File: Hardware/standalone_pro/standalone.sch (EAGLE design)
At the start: 107 parts, among them IC1 STM32F050C6T6A, IC2 AP1212, IC3 AP1212, Q2 32.768khz, U1 NMOS_2N7002, U10 ZXCT1107SA-7, U2 DMS3016SSS-13, U3 DMS3016SSS-13, U4 LM2576S, U5 NMOS_2N7002, U6 NMOS_2N7002, U7 INA213AIDCKT, U9 PMOS_RSS090P03, X1 KUSBVX, X2 KUSBVX, X3 KUSBVX, X4 KUSBVX

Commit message: Standalone pro physical layout finalised
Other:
- note added: "Swap with 1433428C"
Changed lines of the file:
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@@
 <text x="848.36" y="81.28" size="1.778" layer="98">1A Current Limit</text>
 <text x="731.52" y="208.28" size="1.778" layer="98">Add Inv Out</text>
+<text x="259.08" y="396.24" size="1.778" layer="98" rot="R90">Swap with 1433428C</text>
 </plain>
 <instances>

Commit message: Pro Standalone board updated
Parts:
- removed GATE_DRIVE: IR2104S, equinox:IR2104S
- removed KEY_1, KEY_2, KEY_3: 10K, rcl:R-EU_M0805
- removed U$2, U$3, U$4, U$5, U$6: KYCON_KLDVX-0202, equinox:KYCON_KLDVX-0202
- removed U1: NMOS_2N7002, equinox:NMOS_2N7002
- added D1: SSB43L, equinox:DIODE_SSB43L
- added D5: BZX384-C3V6, equinox:BZX384-C3V6
- added DC1, DC2, DC3, DC4, DC5: KYCON_KLDVX-0202, equinox:KYCON_KLDVX-0202
- added IC4: AP1212, equinox:AP1212
- added PTC1: 7A, equinox:PTC_MF_R700
- added R38: 49.9k, resistor:R-EU_M0805
- added U11, U12, U8: NMOS_2N7002, equinox:NMOS_2N7002
- BATT: OC_FARNELL (none) -> 1012166
- BATT_BCKUP: OC_FARNELL (none) -> 1298246
- BUZZ1: device buzzer:BUZZ_14MM -> equinox:BUZZ_14MM
- C21: value 100u -> 100uF; OC_FARNELL (none) -> 1539489
- C22: OC_FARNELL (none) -> 1244342
- C4: OC_FARNELL (none) -> 1539489
- C5: value 0.1uF -> 100nF
- C6: OC_FARNELL (none) -> 9695877
- D2: OC_FARNELL (none) -> 9550216
- D3: value (none) -> SSB43L; OC_FARNELL (none) -> 1336556
- D4: value US1D - 1625280 -> US1D; OC_FARNELL (none) -> 1625280
- D6: OC_FARNELL (none) -> 1843695
- IC1: OC_FARNELL (none) -> 2115059
- IC2: OC_FARNELL (none) -> 1825302
- IC3: value AP1212 -> IR2104S; device equinox:AP1212 -> equinox:IR2104S; OC_FARNELL (none) -> 8638756
- KEYPAD: OC_FARNELL (none) -> 588763
- L_5V: OC_FARNELL (none) -> 1612709
- L_MPPT: OC_FARNELL (none) -> 1929706
- POW: RS (none) -> 758-1979
- Q1: OC_FARNELL (none) -> 2101358
- R1: value 1k -> 75k
- R21: value 1K -> 1k
- R29: value 75k -> 1k
- R31: value 49.9k -> 10M
- R32, R34, R36: value 75k -> 49.9k
- R33, R35, R37: value 49.9k -> 75k
- R4, R6: value 1.32k -> 1.33k
- SOL: TOBY (none) -> DC-001-A-2.1mm-R
- U2, U3: value DMS3016SSS-13 -> FDS6690a; OC_FARNELL (none) -> 9845275
- U4: OC_FARNELL (none) -> 1469178
- U9: OC_FARNELL (none) -> 1525544
- renumbered 5V_CIN to C21, 5V_COUT to C22, Q2 to Q1
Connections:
- removed net LCD_PWR: IC1.PA11, R1.2
- new net N$47: R35.1, R36.2, X4.2
- new net N$48: R37.1, R38.2, X4.3
- net +3V3: no longer KEY_1.2, KEY_2.2, KEY_3.2
- net +5V: now also IC4.IN; no longer IC3.IN
- net 12V_OUT: now also DC1.PAD1, DC2.PAD1, DC3.PAD1; no longer U$2.PAD1, U$3.PAD1, U$4.PAD1
- net 12V_OUT1: now also DC4.PAD1, DC5.PAD1; no longer U$5.PAD1, U$6.PAD1
- net GND: now also CONTR.E, D1.ANODE, D5.A, DC1.PAD2, DC1.PAD3, DC2.PAD2, DC2.PAD3, DC3.PAD2, DC3.PAD3, DC4.PAD2, DC4.PAD3, DC5.PAD2, DC5.PAD3, DIS1.D0, DIS1.D1, DIS1.D2, DIS1.D3, DIS1.GND, IC3.COM, IC4.GND, R32.1, R34.1, R36.1, R38.1, U11.S, U8.S; no longer BUZZ1.-, GATE_DRIVE.COM, IC3.GND, R31.1, R33.1, R35.1, R37.1, U$4.PAD2, U$5.PAD2, U$5.PAD3, U$6.PAD2, U$6.PAD3, U1.S
- net N$10: now also IC3.VB; no longer GATE_DRIVE.VB
- net N$13: now also IC3.LO; no longer GATE_DRIVE.LO
- net N$16: now also IC3.VCC; no longer GATE_DRIVE.VCC
- net N$17: now also R33.1, R34.2, X3.3; no longer R1.1, U1.G
- net N$22: now also R29.1; no longer BUZZ1.+
- net N$23: no longer KEY_1.1
- net N$24: no longer KEY_2.1
- net N$26: no longer KEY_3.1
- net N$3: now also IC3.SD/; no longer GATE_DRIVE.SD/
- net N$4: now also D1.CATHODE, PTC1.P$1; no longer BATTCON$1.S
- net N$42: now also BUZZ1.-, U8.D; no longer R29.1, R31.2, X3.2
- net N$43: now also R29.2, U8.G; no longer R32.1, R33.2, X3.3
- net N$44: now also C16.2, R31.2, U11.G; no longer R34.1, R35.2, X4.2
- net N$45: now also U11.D, U12.S; no longer R36.1, R37.2, X4.3
- net N$46: now also BATTCON$1.S, PTC1.P$2; no longer U$2.PAD2, U$2.PAD3, U$3.PAD2, U$3.PAD3, U$4.PAD3
- net N$5: now also R1.1, R32.2, X3.2; no longer CONTR.E, DIS1.D0, DIS1.D1, DIS1.D2, DIS1.D3, DIS1.GND, U1.D
- net N$6: now also IC3.VS; no longer GATE_DRIVE.VS
- net N$7: now also IC3.HO; no longer GATE_DRIVE.HO
- net N$8: now also IC3.IN; no longer GATE_DRIVE.IN
- net NRST: now also U12.D
- net SOL_I: now also D5.C
- net USB_EN1: now also IC4.EN1; no longer IC3.EN1
- net USB_EN2: now also IC4.EN2; no longer IC3.EN2
- net USB_FLG1: now also IC4.FLG1; no longer IC3.FLG1
- net USB_FLG2: now also IC4.FLG2; no longer IC3.FLG2
- net USB_OUT1: now also IC4.OUT1, R1.2, R33.2; no longer IC3.OUT1, R29.2, R32.2
- net USB_OUT2: now also IC4.OUT2, R35.2, R37.2; no longer IC3.OUT2, R34.2, R36.2
- net V_BACKUP: no longer C16.2
- net V_LOAD: now also BUZZ1.+
- net WKUP: now also R31.1, U12.G
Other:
- note added: "0.5A Current Limit"
- note added: "Must be placed near to IC1"
- note added: "TODO: - Contrast Adjust Pot needs changing - Swap MOS with BJT"
- note removed: "1A Current Limit"
- note removed: "Add Inv Out"
- note removed: "Must be 0placed near to IC1"
- note removed: "Swap with 1433428C"
- note removed: "TODO: - Contrast Adjust Pot needs changing"
- note removed: "Use Internal Pull Ups"
- moved on the sheet: BATTCON$1, BATTCON$2, C11, C16, C19, C2, C20, C3, C5, C6, C8, D2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

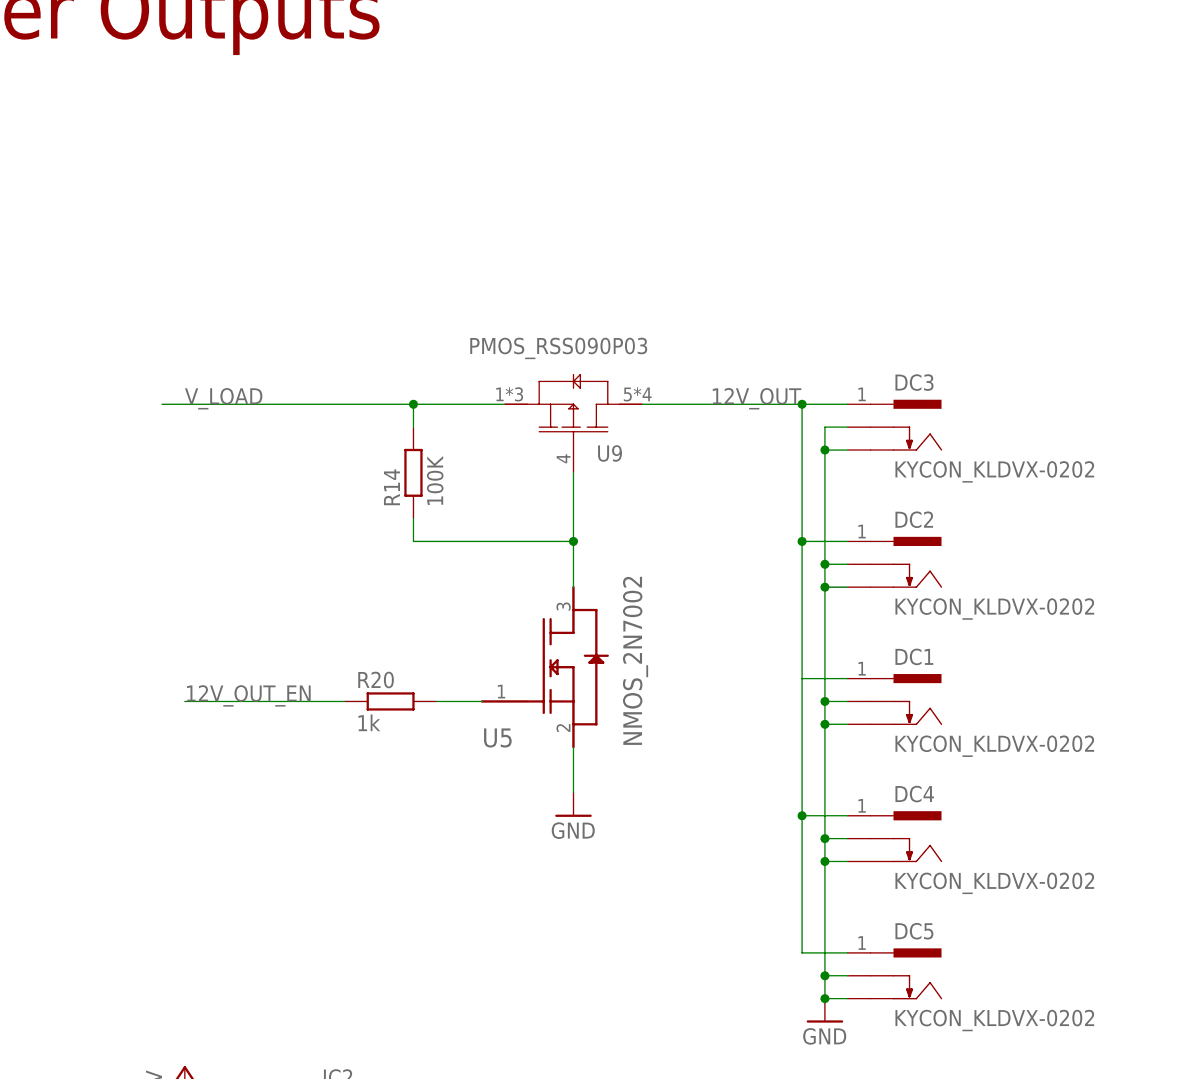
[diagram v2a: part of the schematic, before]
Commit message: Added Relay to Standalone Pro
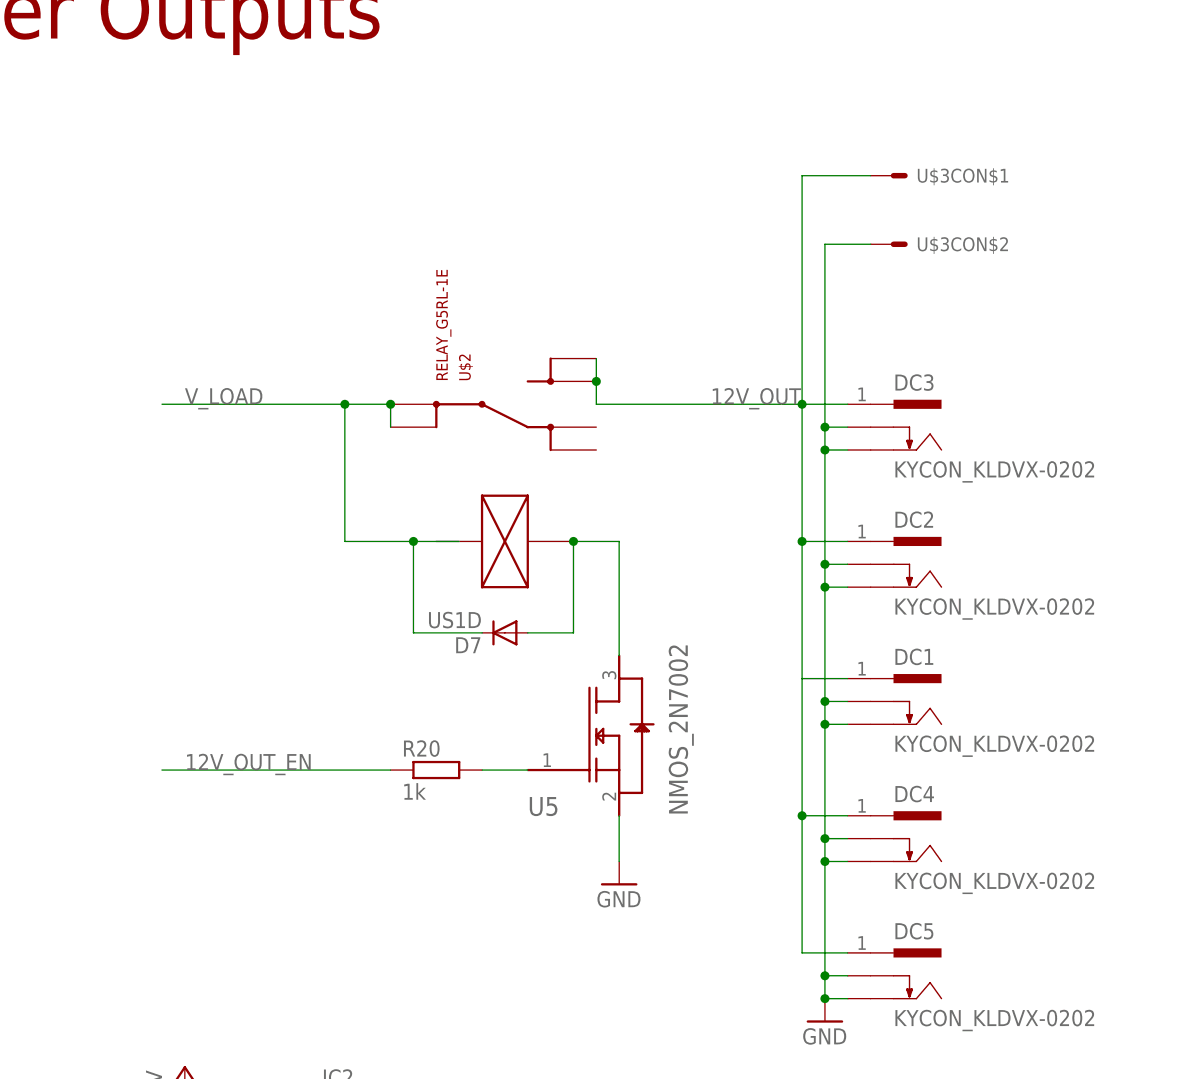
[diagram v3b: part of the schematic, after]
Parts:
- removed R14: 100K, rcl:R-EU_M0805
- removed U9: PMOS_RSS090P03, equinox:PMOS_RSS090P03
- added D7: US1D, diode:DIODE-DO-214AC
- added U$2: RELAY_G5RL-1E, equinox:RELAY_G5RL-1E
- added U$3: CON_MOLEX_39_29_1028, equinox:CON_MOLEX_39_29_1028
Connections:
- removed net N$25: R14.1, U5.D, U9.G
- new net N$50: D7.A, U$2.COIL+, U5.D
- net 12V_OUT: now also U$2.NO@1, U$2.NO@2, U$3CON$1.S; no longer U9.D2
- net GND: now also U$3CON$2.S
- net V_LOAD: now also D7.C, U$2.COM@1, U$2.COM@2; no longer R14.2, U9.S2
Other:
- moved on the sheet: R20, U5
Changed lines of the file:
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@@
 <part name="GND8" library="supply1" deviceset="GND" device="" value="GND"/>
 <part name="P+4" library="supply1" deviceset="+5V" device=""/>
-<part name="U9" library="equinox" deviceset="PMOS_RSS090P03" device="">
-<attribute name="OC_FARNELL" value="1525544"/>
-</part>
-<part name="R14" library="rcl" deviceset="R-EU_" device="M0805" value="100K"/>
 <part name="U5" library="equinox" deviceset="NMOS_2N7002" device=""/>
 <part name="GND10" library="supply1" deviceset="GND" device="" value="GND"/>
@@
 </part>
 <part name="GND35" library="supply1" deviceset="GND" device="" value="GND"/>
+<part name="U$2" library="equinox" deviceset="RELAY_G5RL-1E" device=""/>
+<part name="D7" library="diode" deviceset="DIODE-" device="DO-214AC" value="US1D">
+<attribute name="OC_FARNELL" value="1625280"/>
+</part>
+<part name="U$3" library="equinox" deviceset="CON_MOLEX_39_29_1028" device=""/>
 </parts>
 <sheets>
@@
 <instance part="GND8" gate="1" x="645.16" y="93.98"/>
 <instance part="P+4" gate="1" x="619.76" y="129.54"/>
-<instance part="U9" gate="A" x="660.4" y="200.66" smashed="yes" rot="R270">
-<attribute name="NAME" x="665.48" y="196.85" size="1.778" layer="95"/>
-<attribute name="VALUE" x="651.256" y="208.788" size="1.778" layer="96"/>
-<attribute name="OC_FARNELL" x="660.4" y="200.66" size="1.778" layer="96" rot="R270" display="off"/>
-</instance>
-<instance part="R14" gate="G$1" x="645.16" y="195.58" rot="R90"/>
-<instance part="U5" gate="A" x="660.4" y="175.26"/>
-<instance part="GND10" gate="1" x="662.94" y="157.48"/>
-<instance part="R20" gate="G$1" x="642.62" y="170.18"/>
+<instance part="U5" gate="A" x="665.48" y="167.64"/>
+<instance part="GND10" gate="1" x="668.02" y="149.86"/>
+<instance part="R20" gate="G$1" x="647.7" y="162.56"/>
 <instance part="P+5" gate="1" x="342.9" y="228.6"/>
 <instance part="CONTR" gate="G$1" x="279.4" y="198.12"/>
@@
 </instance>
 <instance part="GND35" gate="1" x="690.88" y="134.62"/>
+<instance part="U$2" gate="G$1" x="655.32" y="198.12" rot="MR90"/>
+<instance part="D7" gate="G$1" x="655.32" y="177.8" rot="R180">
+<attribute name="OC_FARNELL" x="655.32" y="177.8" size="1.778" layer="96" rot="R180" display="off"/>
+</instance>
+<instance part="U$3" gate="CON$1" x="698.5" y="228.6"/>
+<instance part="U$3" gate="CON$2" x="698.5" y="220.98"/>
 </instances>
 <busses>
@@
 </segment>
 <segment>
-<pinref part="U9" gate="A" pin="S2"/>
-<wire x1="655.32" y1="203.2" x2="645.16" y2="203.2" width="0.1524" layer="91"/>
-<pinref part="R14" gate="G$1" pin="2"/>
-<wire x1="645.16" y1="203.2" x2="617.22" y2="203.2" width="0.1524" layer="91"/>
-<wire x1="645.16" y1="200.66" x2="645.16" y2="203.2" width="0.1524" layer="91"/>
-<junction x="645.16" y="203.2"/>
+<wire x1="642.62" y1="203.2" x2="637.54" y2="203.2" width="0.1524" layer="91"/>
 <label x="619.76" y="203.2" size="1.778" layer="95"/>
+<pinref part="U$2" gate="G$1" pin="COM@1"/>
+<pinref part="U$2" gate="G$1" pin="COM@2"/>
+<wire x1="637.54" y1="203.2" x2="617.22" y2="203.2" width="0.1524" layer="91"/>
+<wire x1="642.62" y1="203.2" x2="642.62" y2="200.66" width="0.1524" layer="91"/>
+<junction x="642.62" y="203.2"/>
+<wire x1="650.24" y1="187.96" x2="645.16" y2="187.96" width="0.1524" layer="91"/>
+<wire x1="645.16" y1="187.96" x2="637.54" y2="187.96" width="0.1524" layer="91"/>
+<wire x1="637.54" y1="187.96" x2="637.54" y2="203.2" width="0.1524" layer="91"/>
+<junction x="637.54" y="203.2"/>
+<pinref part="D7" gate="G$1" pin="C"/>
+<wire x1="652.78" y1="177.8" x2="645.16" y2="177.8" width="0.1524" layer="91"/>
+<wire x1="645.16" y1="177.8" x2="645.16" y2="187.96" width="0.1524" layer="91"/>
+<junction x="645.16" y="187.96"/>
 </segment>
 <segment>
@@
 <pinref part="DC1" gate="G$1" pin="PAD1"/>
 <wire x1="688.34" y1="172.72" x2="693.42" y2="172.72" width="0.1524" layer="91"/>
-<wire x1="688.34" y1="203.2" x2="670.56" y2="203.2" width="0.1524" layer="91"/>
+<wire x1="688.34" y1="203.2" x2="665.48" y2="203.2" width="0.1524" layer="91"/>
 <junction x="688.34" y="203.2"/>
 <label x="678.18" y="203.2" size="1.778" layer="95"/>
-<pinref part="U9" gate="A" pin="D2"/>
+<pinref part="U$2" gate="G$1" pin="NO@1"/>
+<wire x1="665.48" y1="203.2" x2="665.48" y2="205.74" width="0.1524" layer="91"/>
+<pinref part="U$2" gate="G$1" pin="NO@2"/>
+<wire x1="665.48" y1="208.28" x2="665.48" y2="205.74" width="0.1524" layer="91"/>
+<junction x="665.48" y="205.74"/>
+<wire x1="688.34" y1="203.2" x2="688.34" y2="228.6" width="0.1524" layer="91"/>
+<pinref part="U$3" gate="CON$1" pin="S"/>
+<wire x1="688.34" y1="228.6" x2="695.96" y2="228.6" width="0.1524" layer="91"/>
 </segment>
 </net>
@@
 <segment>
 <pinref part="R20" gate="G$1" pin="1"/>
-<wire x1="637.54" y1="170.18" x2="619.76" y2="170.18" width="0.1524" layer="91"/>
-<label x="619.76" y="170.18" size="1.778" layer="95"/>
+<wire x1="642.62" y1="162.56" x2="617.22" y2="162.56" width="0.1524" layer="91"/>
+<label x="619.76" y="162.56" size="1.778" layer="95"/>
 </segment>
 </net>
@@
 </segment>
 </net>
-<net name="N$25" class="0">
-<segment>
-<pinref part="R14" gate="G$1" pin="1"/>
-<wire x1="645.16" y1="190.5" x2="645.16" y2="187.96" width="0.1524" layer="91"/>
-<pinref part="U9" gate="A" pin="G"/>
-<wire x1="645.16" y1="187.96" x2="662.94" y2="187.96" width="0.1524" layer="91"/>
-<wire x1="662.94" y1="187.96" x2="662.94" y2="195.58" width="0.1524" layer="91"/>
-<pinref part="U5" gate="A" pin="D"/>
-<wire x1="662.94" y1="182.88" x2="662.94" y2="187.96" width="0.1524" layer="91"/>
-<junction x="662.94" y="187.96"/>
-</segment>
-</net>
 <net name="N$35" class="0">
 <segment>
 <pinref part="R20" gate="G$1" pin="2"/>
 <pinref part="U5" gate="A" pin="G"/>
-<wire x1="647.7" y1="170.18" x2="652.78" y2="170.18" width="0.1524" layer="91"/>
+<wire x1="652.78" y1="162.56" x2="657.86" y2="162.56" width="0.1524" layer="91"/>
 </segment>
 </net>
@@
 <segment>
 <pinref part="U5" gate="A" pin="S"/>
-<wire x1="662.94" y1="165.1" x2="662.94" y2="160.02" width="0.1524" layer="91"/>
+<wire x1="668.02" y1="157.48" x2="668.02" y2="152.4" width="0.1524" layer="91"/>
 <pinref part="GND10" gate="1" pin="GND"/>
 </segment>
@@
 <wire x1="693.42" y1="167.64" x2="690.88" y2="167.64" width="0.1524" layer="91"/>
 <junction x="690.88" y="167.64"/>
+<pinref part="U$3" gate="CON$2" pin="S"/>
+<wire x1="695.96" y1="220.98" x2="690.88" y2="220.98" width="0.1524" layer="91"/>
+<wire x1="690.88" y1="220.98" x2="690.88" y2="200.66" width="0.1524" layer="91"/>
+<junction x="690.88" y="200.66"/>
 </segment>
 </net>
@@
 </segment>
 </net>
+<net name="N$50" class="0">
+<segment>
+<pinref part="U$2" gate="G$1" pin="COIL+"/>
+<pinref part="U5" gate="A" pin="D"/>
+<wire x1="662.94" y1="187.96" x2="668.02" y2="187.96" width="0.1524" layer="91"/>
+<wire x1="668.02" y1="187.96" x2="668.02" y2="175.26" width="0.1524" layer="91"/>
+<pinref part="D7" gate="G$1" pin="A"/>
+<wire x1="657.86" y1="177.8" x2="662.94" y2="177.8" width="0.1524" layer="91"/>
+<wire x1="662.94" y1="177.8" x2="662.94" y2="187.96" width="0.1524" layer="91"/>
+<junction x="662.94" y="187.96"/>
+</segment>
+</net>

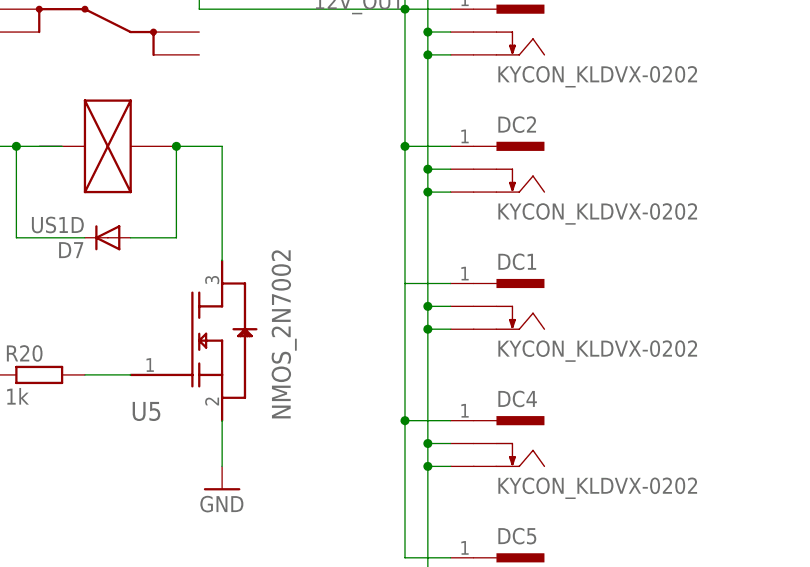
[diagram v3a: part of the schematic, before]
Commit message: Connections added (with corrected faults)
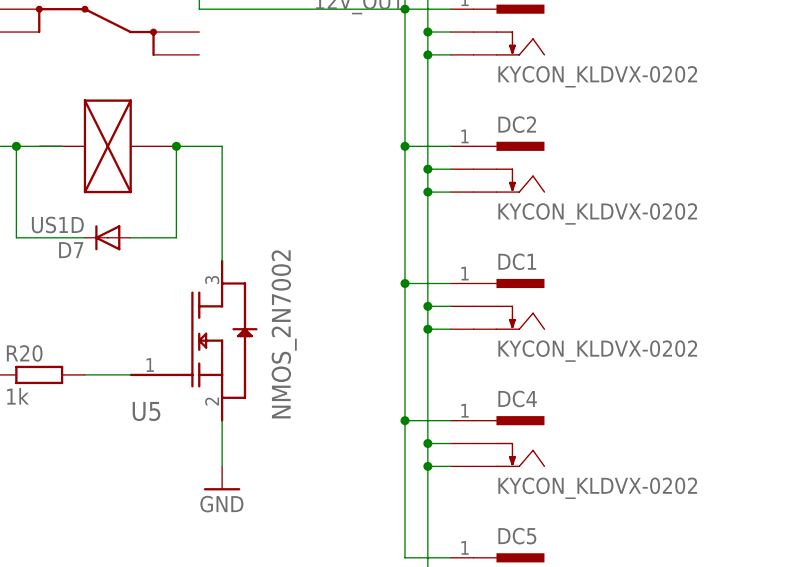
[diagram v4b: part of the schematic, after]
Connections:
- removed net 12V_OUT1: DC4.PAD1, DC5.PAD1
- net 12V_OUT: now also DC4.PAD1, DC5.PAD1
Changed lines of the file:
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@@
 <?xml version="1.0" encoding="utf-8"?>
 <!DOCTYPE eagle SYSTEM "eagle.dtd">
-<eagle version="6.3">
+<eagle version="6.4">
 <drawing>
 <settings>
@@
 <pinref part="U$3" gate="CON$1" pin="S"/>
 <wire x1="688.34" y1="228.6" x2="695.96" y2="228.6" width="0.1524" layer="91"/>
+<pinref part="DC4" gate="G$1" pin="PAD1"/>
+<wire x1="693.42" y1="157.48" x2="688.34" y2="157.48" width="0.1524" layer="91"/>
+<wire x1="688.34" y1="157.48" x2="688.34" y2="172.72" width="0.1524" layer="91"/>
+<wire x1="688.34" y1="142.24" x2="688.34" y2="157.48" width="0.1524" layer="91"/>
+<junction x="688.34" y="157.48"/>
+<pinref part="DC5" gate="G$1" pin="PAD1"/>
+<wire x1="688.34" y1="142.24" x2="693.42" y2="142.24" width="0.1524" layer="91"/>
+<junction x="688.34" y="172.72"/>
 </segment>
 </net>
@@
 </segment>
 </net>
-<net name="12V_OUT1" class="2">
-<segment>
-<pinref part="DC4" gate="G$1" pin="PAD1"/>
-<wire x1="693.42" y1="157.48" x2="688.34" y2="157.48" width="0.1524" layer="91"/>
-<wire x1="688.34" y1="157.48" x2="688.34" y2="172.72" width="0.1524" layer="91"/>
-<wire x1="688.34" y1="142.24" x2="688.34" y2="157.48" width="0.1524" layer="91"/>
-<junction x="688.34" y="157.48"/>
-<pinref part="DC5" gate="G$1" pin="PAD1"/>
-<wire x1="688.34" y1="142.24" x2="693.42" y2="142.24" width="0.1524" layer="91"/>
-</segment>
-</net>
